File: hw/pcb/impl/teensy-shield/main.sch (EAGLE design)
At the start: 37 parts, among them J1 JS202011SCQN, Q1 2N7002, Q2 2N7002, Q3 2N7002, U1 MCP73831-SOT5, U2 MAX17040-TDFN, U3 SPBT2632C2A

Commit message: removed all the stuff we're not using from board
The fuel gauge IC, the crummy camera JST connectors, everything
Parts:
- removed C3: 1uF, resistor:C-EUC0402
- removed JP6: LED, SparkFun:M02LOCK_LONGPADS
- removed JP7, JP8: SM08B-ZESS-TB, glasses:SM08B-ZESS-TB
- removed Q3: 2N7002, SparkFun:MOSFET-NCHANNELSMD
- removed R5: DNI, resistor:R-US_R0402
- removed U2: MAX17040-TDFN, glasses:MAX17040-TDFN
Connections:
- removed net I2C_SCL: JP3.7, U2.SCL
- removed net I2C_SDA: JP3.6, U2.SDA
- removed net IR_LED: JP2.4, Q3.G
- removed net N$11: JP6.1, R5.1
- removed net N$12: Q3.D, R5.2
- removed net N$6: U3.CTS, U3.RTS
- removed net SPI_CS: JP2.3, U3.GPIO4/SS
- removed net SPI_MISO: JP2.1, U3.GPIO1/MISO
- removed net SPI_MOSI: JP2.2, U3.GPIO2/MOSI
- removed net SPI_SCK: JP3.2, U3.GPIO3/SCLK
- new net CTS: JP3.7, U3.CTS
- new net RTS: JP3.6, U3.RTS
- new net TS_GP10: JP2.3
- new net TS_GP11: JP2.2
- new net TS_GP12: JP2.1
- new net TS_GP14: JP3.2
- new net TS_GP9: JP2.4
- net +3V3: no longer JP6.2
- net GND: no longer C3.1, JP7.P7, JP8.P2, Q3.S, U2.CTG, U2.EO, U2.EP, U2.GND, U2.SEO
- net INCP: no longer JP7.P2, JP8.P7
- net INCV: no longer JP7.P4, JP8.P5
- net INPHI: no longer JP7.P5, JP8.P4
- net PIXEL_EYE: no longer JP7.P8
- net PIXEL_FRONT: no longer JP8.P1
- net RESP: no longer JP7.P1, JP8.P8
- net RESV: no longer JP7.P3, JP8.P6
- net VBAT: no longer U2.CELL
- net VCCIO: no longer C3.2, JP7.P6, JP8.P3, U2.VDD

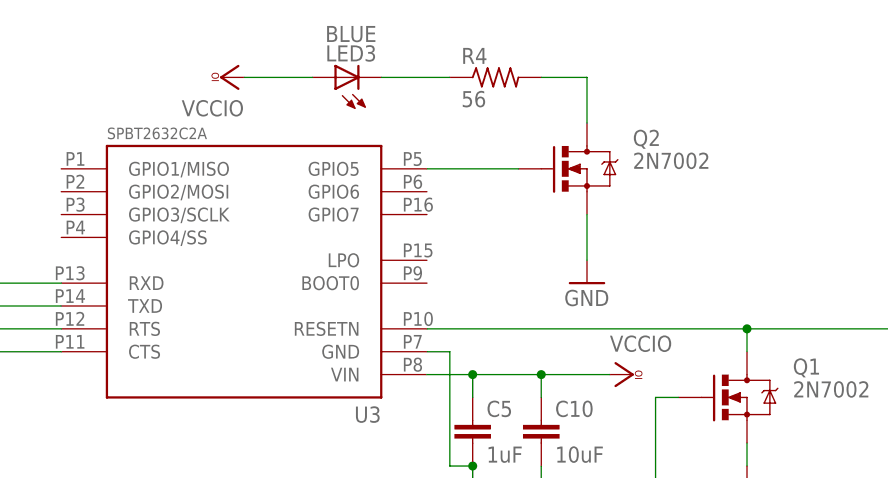
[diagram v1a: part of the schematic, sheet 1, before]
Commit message: finished re-routing the board
removed the stuff that wasn't used, fixing the bluetooth module's
footprint and routing RTS and CTS.
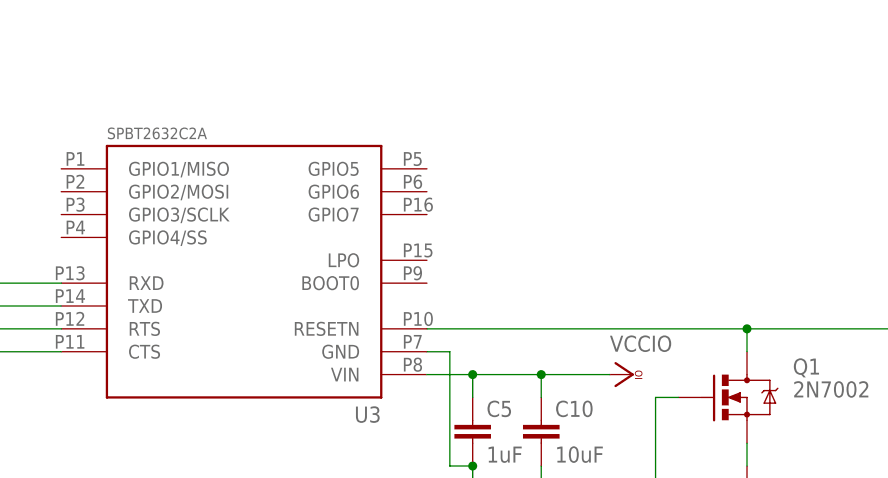
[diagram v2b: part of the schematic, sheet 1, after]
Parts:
- removed LED3: BLUE, led:LEDCHIPLED_0603
- removed Q2: 2N7002, SparkFun:MOSFET-NCHANNELSMD
- removed R4: 56, resistor:R-US_R0402
- C1, C8, C9: device resistor:C-EUC0402 -> rcl:C-EUC0603
- C2: value 1uF -> 10uF; device resistor:C-EUC0402 -> rcl:C-EUC0603
- C7: value 10uF -> 1uF
- R3: device resistor:R-US_R0402 -> rcl:R-US_R0603
- U3: device glasses:SPBT2632C2A -> senseye:SPBT2632C2A
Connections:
- removed net N$10: Q2.D, R4.2
- removed net N$8: Q2.G, U3.GPIO5
- removed net N$9: LED3.C, R4.1
- net GND: no longer Q2.S
- net VCCIO: no longer LED3.A
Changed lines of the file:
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@@
 <part name="GND3" library="supply1" deviceset="GND" device=""/>
 <part name="GND4" library="supply1" deviceset="GND" device=""/>
-<part name="C1" library="resistor" deviceset="C-EU" device="C0402" value="1uF"/>
-<part name="C2" library="resistor" deviceset="C-EU" device="C0402" value="1uF"/>
+<part name="C1" library="rcl" deviceset="C-EU" device="C0603" value="1uF"/>
+<part name="C2" library="rcl" deviceset="C-EU" device="C0603" value="10uF"/>
 <part name="U1" library="glasses" deviceset="MCP73831-SOT5" device=""/>
 <part name="R1" library="resistor" deviceset="R-US_" device="R0402" value="150"/>
@@
 <part name="J1" library="glasses" deviceset="JS202011SCQN" device=""/>
 <part name="LED2" library="led" deviceset="LED" device="CHIPLED_0603" value="GREEN"/>
-<part name="R3" library="resistor" deviceset="R-US_" device="R0402" value="56"/>
+<part name="R3" library="rcl" deviceset="R-US_" device="R0603" value="56"/>
 <part name="GND9" library="supply1" deviceset="GND" device=""/>
 <part name="JP2" library="SparkFun" deviceset="M14" device="LOCK"/>
@@
 <part name="JP4" library="SparkFun" deviceset="M05" device="LOCK"/>
 <part name="JP5" library="SparkFun" deviceset="M01" device="PTH"/>
-<part name="U3" library="glasses" deviceset="SPBT2632C2A" device=""/>
+<part name="U3" library="senseye" deviceset="SPBT2632C2A" device=""/>
 <part name="VCC1" library="supply1" deviceset="VCCIO" device=""/>
 <part name="GND10" library="supply1" deviceset="GND" device=""/>
@@
 <part name="C6" library="resistor" deviceset="C-EU" device="C0603" value="10uF"/>
 <part name="GND16" library="supply1" deviceset="GND" device=""/>
-<part name="C7" library="resistor" deviceset="C-EU" device="C0603" value="10uF"/>
+<part name="C7" library="resistor" deviceset="C-EU" device="C0603" value="1uF"/>
 <part name="GND17" library="supply1" deviceset="GND" device=""/>
-<part name="Q2" library="SparkFun" deviceset="MOSFET-NCHANNEL" device="SMD" value="2N7002"/>
-<part name="GND18" library="supply1" deviceset="GND" device=""/>
-<part name="R4" library="resistor" deviceset="R-US_" device="R0402" value="56"/>
-<part name="LED3" library="led" deviceset="LED" device="CHIPLED_0603" value="BLUE"/>
 <part name="GND19" library="supply1" deviceset="GND" device=""/>
 <part name="GND21" library="supply1" deviceset="GND" device=""/>
-<part name="C8" library="resistor" deviceset="C-EU" device="C0402" value="0.1uF"/>
+<part name="C8" library="rcl" deviceset="C-EU" device="C0603" value="0.1uF"/>
 <part name="GND22" library="supply1" deviceset="GND" device=""/>
-<part name="C9" library="resistor" deviceset="C-EU" device="C0402" value="0.1uF"/>
+<part name="C9" library="rcl" deviceset="C-EU" device="C0603" value="0.1uF"/>
 <part name="VCC3" library="supply1" deviceset="VCCIO" device=""/>
-<part name="VCC4" library="supply1" deviceset="VCCIO" device=""/>
 <part name="+3V1" library="supply1" deviceset="+3V3" device=""/>
 <part name="RESET" library="glasses" deviceset="EVP-AA202K_BUTTON" device=""/>
@@
 <instance part="C5" gate="G$1" x="91.44" y="48.26"/>
 <instance part="GND15" gate="1" x="91.44" y="38.1"/>
-<instance part="Q2" gate="G$1" x="104.14" y="76.2"/>
-<instance part="GND18" gate="1" x="104.14" y="63.5"/>
-<instance part="R4" gate="G$1" x="93.98" y="86.36"/>
-<instance part="LED3" gate="G$1" x="76.2" y="86.36" rot="R90"/>
 <instance part="GND21" gate="1" x="53.34" y="5.08"/>
 <instance part="C8" gate="G$1" x="35.56" y="22.86" rot="R90"/>
@@
 <instance part="C9" gate="G$1" x="93.98" y="22.86" rot="R90"/>
 <instance part="VCC3" gate="G$1" x="109.22" y="53.34" rot="R270"/>
-<instance part="VCC4" gate="G$1" x="63.5" y="86.36" rot="R90"/>
 <instance part="RESET" gate="G$1" x="35.56" y="17.78"/>
 <instance part="PROGRAM" gate="G$1" x="93.98" y="17.78"/>
@@
 </segment>
 <segment>
-<pinref part="Q2" gate="G$1" pin="S"/>
-<pinref part="GND18" gate="1" pin="GND"/>
-<wire x1="104.14" y1="71.12" x2="104.14" y2="66.04" width="0.1524" layer="91"/>
-</segment>
-<segment>
 <pinref part="GND21" gate="1" pin="GND"/>
 <wire x1="48.26" y1="15.24" x2="53.34" y2="15.24" width="0.1524" layer="91"/>
@@
 <wire x1="139.7" y1="58.42" x2="139.7" y2="55.88" width="0.1524" layer="91"/>
 <junction x="121.92" y="58.42"/>
-</segment>
-</net>
-<net name="N$8" class="0">
-<segment>
-<pinref part="U3" gate="G$1" pin="GPIO5"/>
-<pinref part="Q2" gate="G$1" pin="G"/>
-<wire x1="86.36" y1="76.2" x2="96.52" y2="76.2" width="0.1524" layer="91"/>
-</segment>
-</net>
-<net name="N$9" class="0">
-<segment>
-<pinref part="LED3" gate="G$1" pin="C"/>
-<pinref part="R4" gate="G$1" pin="1"/>
-<wire x1="81.28" y1="86.36" x2="88.9" y2="86.36" width="0.1524" layer="91"/>
-</segment>
-</net>
-<net name="N$10" class="0">
-<segment>
-<pinref part="R4" gate="G$1" pin="2"/>
-<pinref part="Q2" gate="G$1" pin="D"/>
-<wire x1="99.06" y1="86.36" x2="104.14" y2="86.36" width="0.1524" layer="91"/>
-<wire x1="104.14" y1="86.36" x2="104.14" y2="81.28" width="0.1524" layer="91"/>
 </segment>
 </net>
@@
 <junction x="99.06" y="53.34"/>
 </segment>
-<segment>
-<pinref part="LED3" gate="G$1" pin="A"/>
-<wire x1="66.04" y1="86.36" x2="73.66" y2="86.36" width="0.1524" layer="91"/>
-<pinref part="VCC4" gate="G$1" pin="VCCIO"/>
-</segment>
 </net>
